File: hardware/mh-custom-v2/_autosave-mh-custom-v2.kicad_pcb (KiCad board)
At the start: 2 copper layers, 95.7 x 99.3 mm, 107 parts, among them J1 Conn_01x03_Male, J3 Conn_02x19_Top_Bottom, J4 Conn_02x19_Top_Bottom, J5 Screw_Terminal_01x04, J6 Screw_Terminal_01x04, J7 Screw_Terminal_01x04, J8 Screw_Terminal_01x04, SW1 SW_DIP_x04, T1 AO3400A, T2 AO3400A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

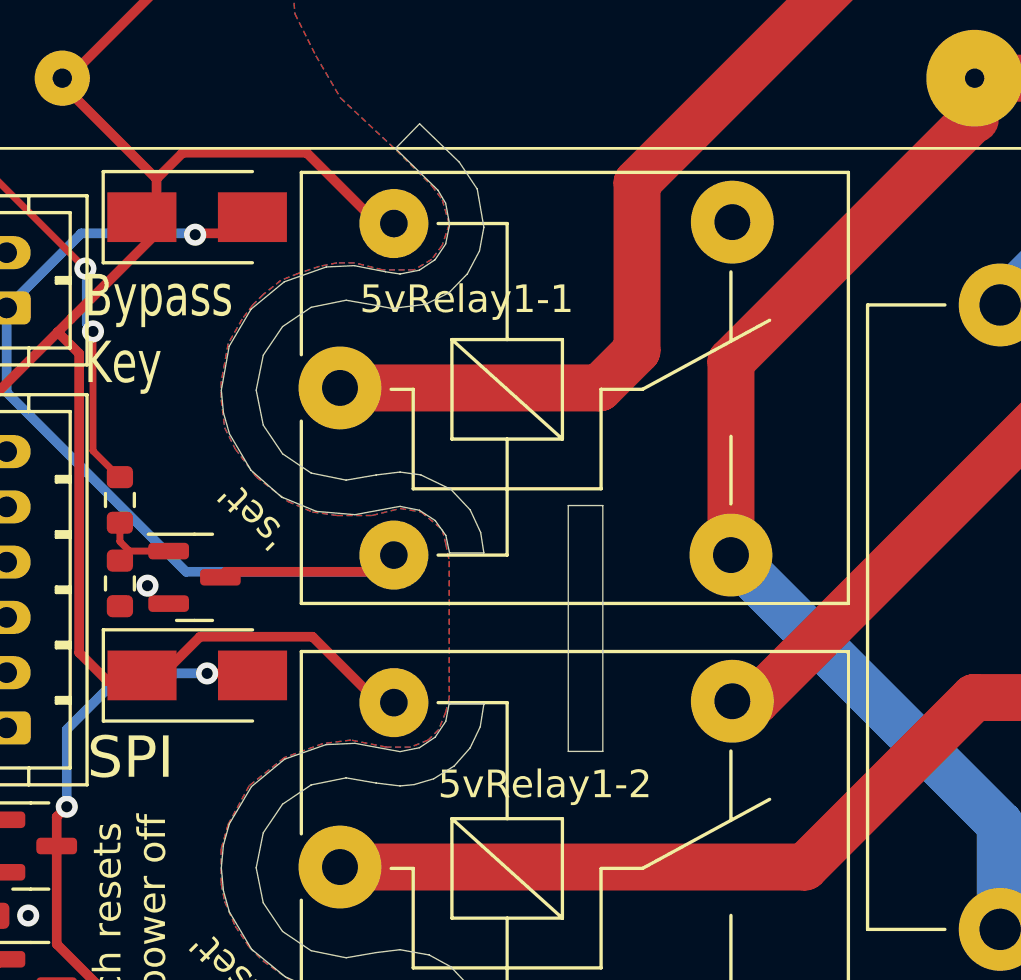
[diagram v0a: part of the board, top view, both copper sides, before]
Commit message: finalizing details of ordering from JLCPCB
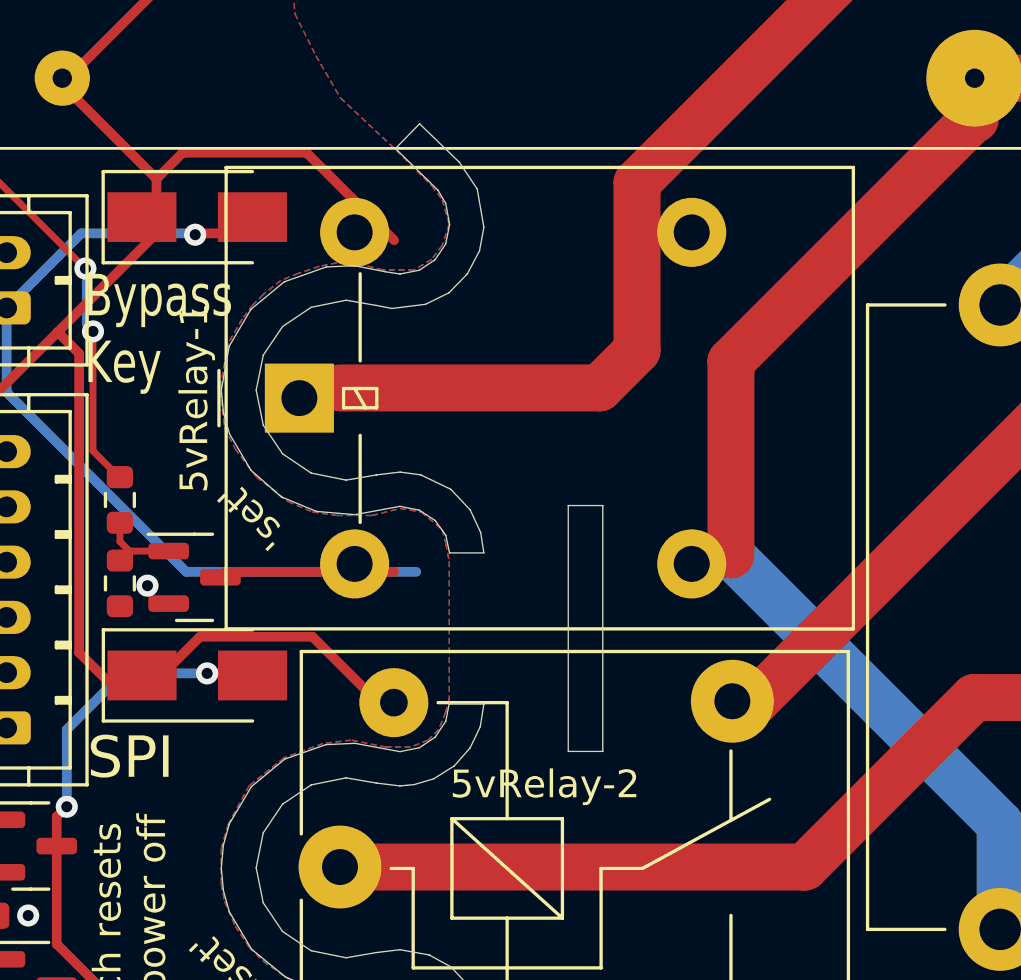
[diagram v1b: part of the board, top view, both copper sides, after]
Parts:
- 5vRelay-1: renamed from 5vRelay1-1; value SANYOU_SRD_Form_C -> JQC-3FF/005-1ZS(551); footprint Relay_THT:Relay_SPDT_SANYOU_SRD_Series_Form_C -> Relay_THT:Relay_SPDT_Omron-G5LE-1
- 5vRelay-2: renamed from 5vRelay1-2; value SANYOU_SRD_Form_C -> JQC-3FF/005-1ZS(551)
- moved 5vRelay-1 1.52 mm to (81.0, 62.4), turned to 90 degrees
